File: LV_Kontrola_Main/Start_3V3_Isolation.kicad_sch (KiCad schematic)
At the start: 56 parts, among them IC10 UCC12040DVE, IC12 UCC12040DVE, IC14 UCC12040DVE, IC16 UCC12040DVE, IC2 UCC12040DVE, IC4 UCC12040DVE, IC6 UCC12040DVE, IC8 UCC12040DVE

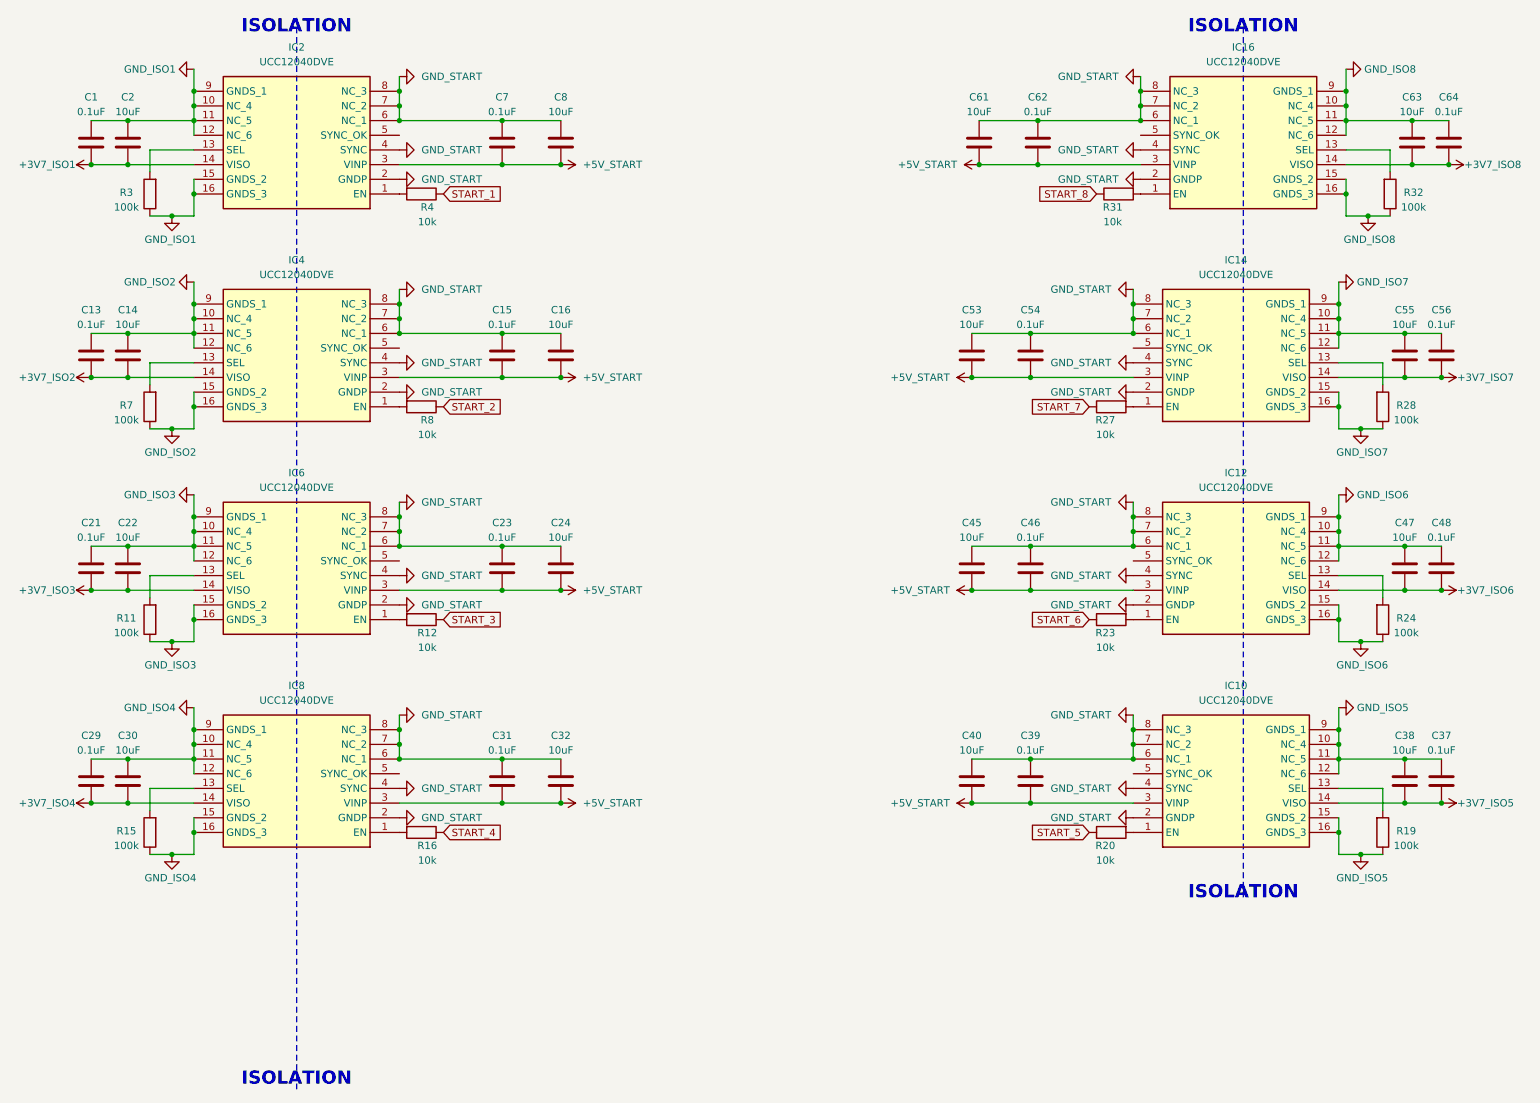
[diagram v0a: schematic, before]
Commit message: Changes to LV_Kontrola_Main
Added a lot to the schematic, fixed component libs, mics...
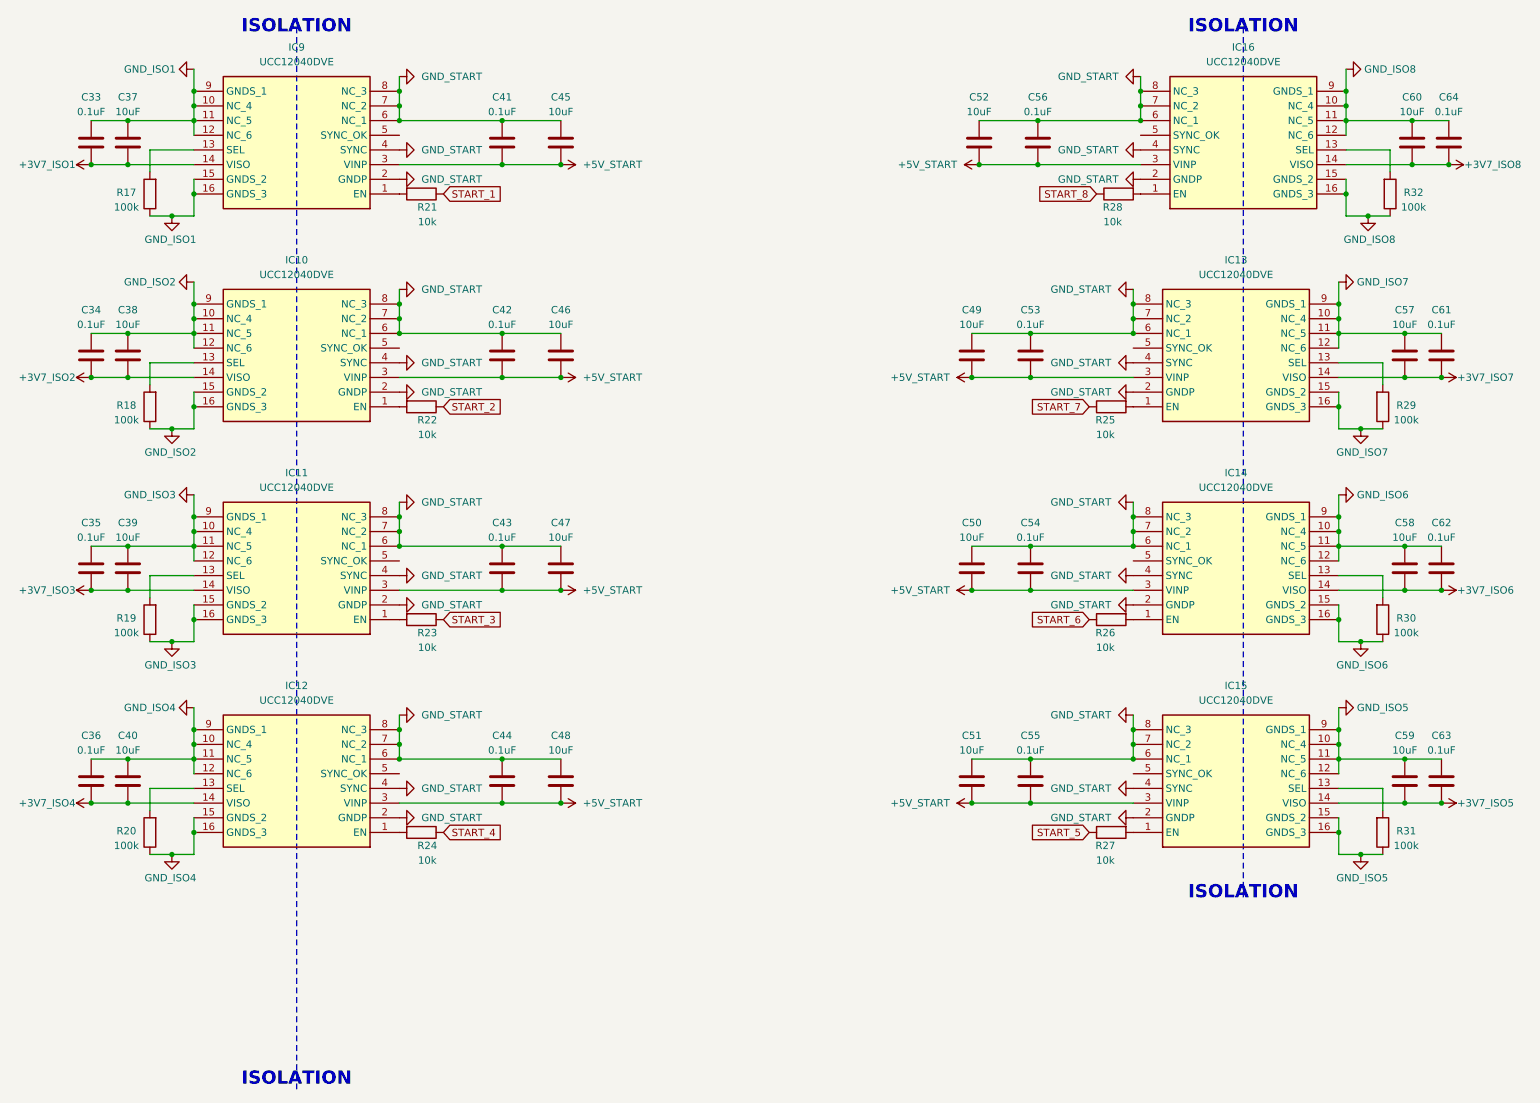
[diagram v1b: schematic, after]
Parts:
- renumbered C1 to C33, C13 to C34, C21 to C35, C29 to C36, C2 to C37, C14 to C38, C22 to C39, C30 to C40, C7 to C41, C15 to C42, C23 to C43, C31 to C44, C8 to C45, C16 to C46, C24 to C47, C32 to C48, C53 to C49, C45 to C50, C40 to C51, C61 to C52, C54 to C53, C46 to C54, C39 to C55, C62 to C56, C55 to C57, C47 to C58, C38 to C59, C63 to C60, C56 to C61, C48 to C62, C37 to C63, IC4 to IC10, IC6 to IC11, IC8 to IC12, IC14 to IC13, IC12 to IC14, IC10 to IC15, IC2 to IC9, R3 to R17, R7 to R18, R11 to R19, R15 to R20, R4 to R21, R8 to R22, R12 to R23, R16 to R24, R27 to R25, R23 to R26, R20 to R27, R31 to R28, R28 to R29, R24 to R30, R19 to R31
